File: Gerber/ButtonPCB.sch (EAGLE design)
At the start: 7 parts, among them SW1 SPST_TACT-EVQQ2, SW2 SPST_TACT-EVQQ2, SW3 SPST_TACT-EVQQ2

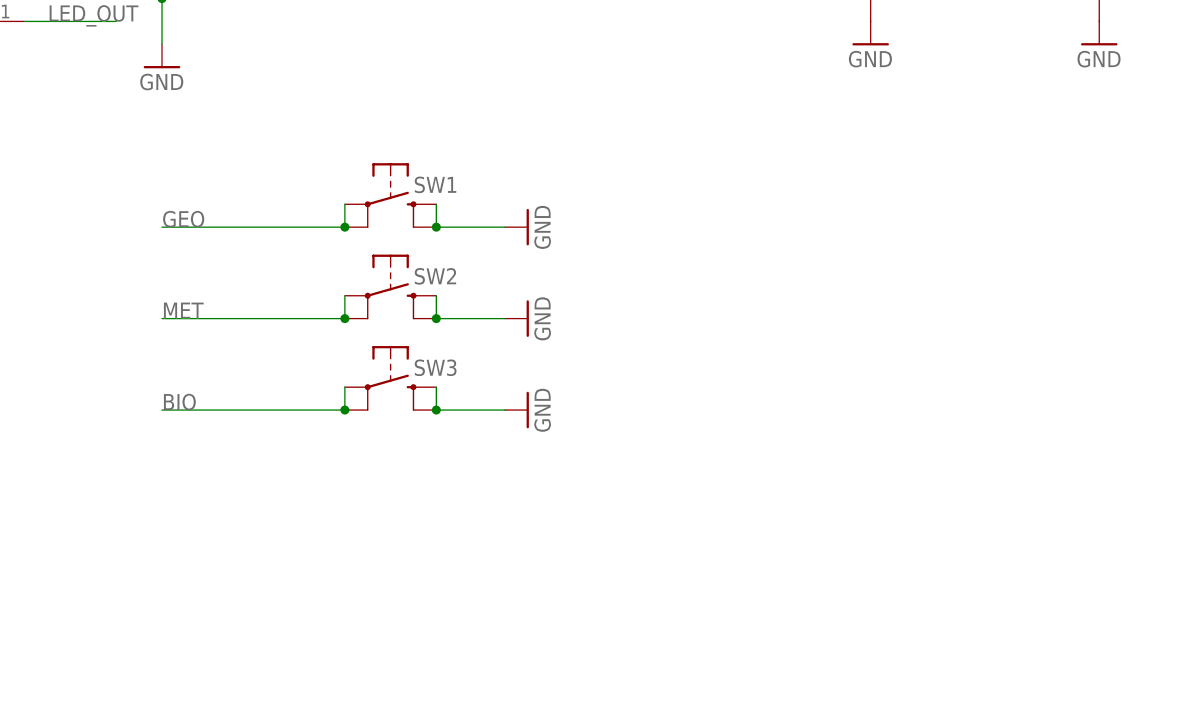
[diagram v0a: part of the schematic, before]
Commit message: Swapped to smd buttons that I like.
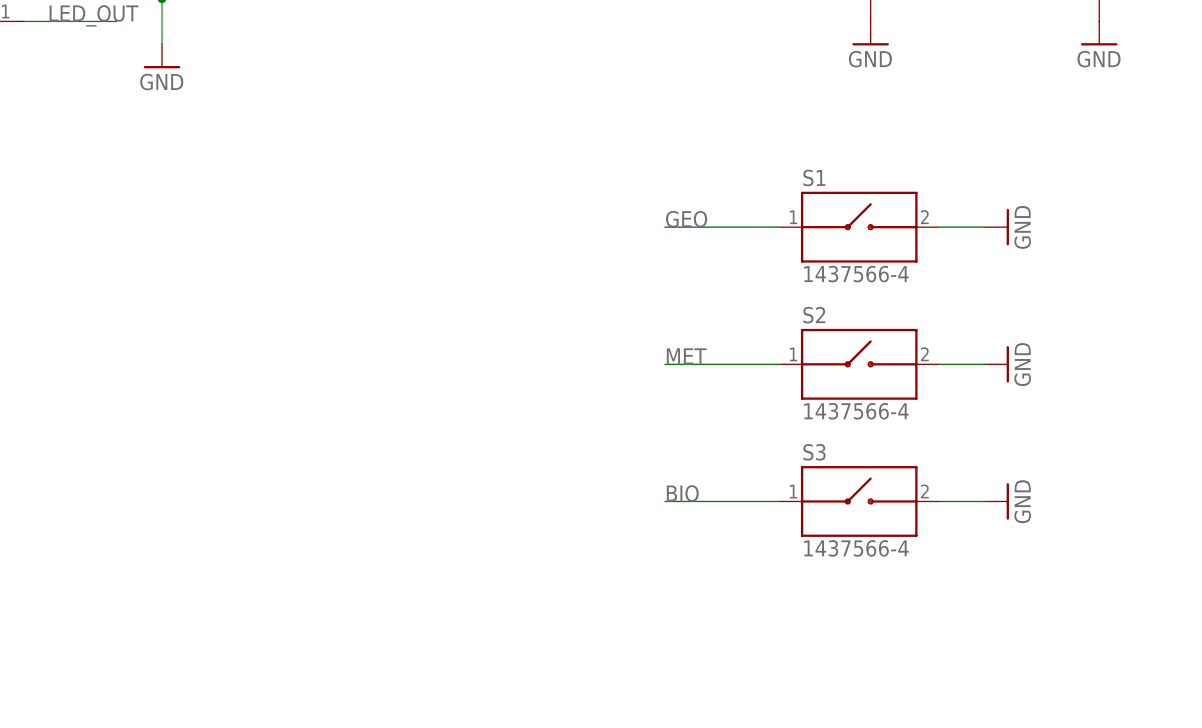
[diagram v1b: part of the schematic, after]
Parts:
- removed SW1, SW2, SW3: SPST_TACT-EVQQ2, microbuilder:SWITCH_TACT_SMT4.6X2.8
- added S1, S2, S3: 1437566-4, FSMSMTR-1437566-4:1437566-4
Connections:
- net BIO: now also S3.1; no longer SW3.P, SW3.P1
- net GEO: now also S1.1; no longer SW1.P, SW1.P1
- net GND: now also S1.2, S2.2, S3.2; no longer SW1.S, SW1.S1, SW2.S, SW2.S1, SW3.S, SW3.S1
- net MET: now also S2.1; no longer SW2.P, SW2.P1
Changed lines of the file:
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@@
 <part name="GND4" library="supply1a" deviceset="GND" device=""/>
 <part name="P+3" library="supply1" deviceset="V+" device=""/>
-<part name="GND22" library="supply1a" deviceset="GND" device=""/>
-<part name="SW1" library="microbuilder" deviceset="SWITCH_TACT_SMT" device="4.6X2.8" value="SPST_TACT-EVQQ2"/>
-<part name="GND1" library="supply1a" deviceset="GND" device=""/>
-<part name="SW2" library="microbuilder" deviceset="SWITCH_TACT_SMT" device="4.6X2.8" value="SPST_TACT-EVQQ2"/>
-<part name="GND2" library="supply1a" deviceset="GND" device=""/>
-<part name="SW3" library="microbuilder" deviceset="SWITCH_TACT_SMT" device="4.6X2.8" value="SPST_TACT-EVQQ2"/>
 <part name="J1" library="SparkFun-Connectors" deviceset="CONN_09" device=""/>
 <part name="P+1" library="supply1" deviceset="V+" device=""/>
 <part name="GND5" library="supply1a" deviceset="GND" device=""/>
+<part name="S1" library="FSMSMTR-1437566-4" deviceset="1437566-4" device=""/>
+<part name="S2" library="FSMSMTR-1437566-4" deviceset="1437566-4" device=""/>
+<part name="S3" library="FSMSMTR-1437566-4" deviceset="1437566-4" device=""/>
+<part name="GND6" library="supply1a" deviceset="GND" device=""/>
+<part name="GND7" library="supply1a" deviceset="GND" device=""/>
+<part name="GND8" library="supply1a" deviceset="GND" device=""/>
 </parts>
 <sheets>
@@
 <attribute name="VALUE" x="182.88" y="160.02" size="1.778" layer="96" rot="R90"/>
 </instance>
-<instance part="GND22" gate="1" x="91.44" y="111.76" smashed="yes" rot="R90">
-<attribute name="VALUE" x="93.98" y="109.22" size="1.778" layer="96" rot="R90"/>
-</instance>
-<instance part="SW1" gate="G$1" x="76.2" y="114.3" smashed="yes">
-<attribute name="NAME" x="78.74" y="115.57" size="1.778" layer="95"/>
-</instance>
-<instance part="GND1" gate="1" x="91.44" y="101.6" smashed="yes" rot="R90">
-<attribute name="VALUE" x="93.98" y="99.06" size="1.778" layer="96" rot="R90"/>
-</instance>
-<instance part="SW2" gate="G$1" x="76.2" y="104.14" smashed="yes">
-<attribute name="NAME" x="78.74" y="105.41" size="1.778" layer="95"/>
-</instance>
-<instance part="GND2" gate="1" x="91.44" y="91.44" smashed="yes" rot="R90">
-<attribute name="VALUE" x="93.98" y="88.9" size="1.778" layer="96" rot="R90"/>
-</instance>
-<instance part="SW3" gate="G$1" x="76.2" y="93.98" smashed="yes">
-<attribute name="NAME" x="78.74" y="95.25" size="1.778" layer="95"/>
-</instance>
 <instance part="J1" gate="J1" x="25.4" y="144.78"/>
 <instance part="P+1" gate="1" x="48.26" y="162.56" smashed="yes">
@@
 <instance part="GND5" gate="1" x="50.8" y="129.54" smashed="yes">
 <attribute name="VALUE" x="48.26" y="127" size="1.778" layer="96"/>
+</instance>
+<instance part="S1" gate="G$1" x="127" y="111.76"/>
+<instance part="S2" gate="G$1" x="127" y="96.52"/>
+<instance part="S3" gate="G$1" x="127" y="81.28"/>
+<instance part="GND6" gate="1" x="144.78" y="111.76" smashed="yes" rot="R90">
+<attribute name="VALUE" x="147.32" y="109.22" size="1.778" layer="96" rot="R90"/>
+</instance>
+<instance part="GND7" gate="1" x="144.78" y="96.52" smashed="yes" rot="R90">
+<attribute name="VALUE" x="147.32" y="93.98" size="1.778" layer="96" rot="R90"/>
+</instance>
+<instance part="GND8" gate="1" x="144.78" y="81.28" smashed="yes" rot="R90">
+<attribute name="VALUE" x="147.32" y="78.74" size="1.778" layer="96" rot="R90"/>
 </instance>
 </instances>
@@
 <pinref part="LED3" gate="G$1" pin="GND"/>
 <pinref part="GND4" gate="1" pin="GND"/>
-</segment>
-<segment>
-<wire x1="88.9" y1="111.76" x2="81.28" y2="111.76" width="0.1524" layer="91"/>
-<wire x1="81.28" y1="114.3" x2="81.28" y2="111.76" width="0.1524" layer="91"/>
-<junction x="81.28" y="111.76"/>
-<pinref part="GND22" gate="1" pin="GND"/>
-<pinref part="SW1" gate="G$1" pin="S"/>
-<pinref part="SW1" gate="G$1" pin="S1"/>
-</segment>
-<segment>
-<wire x1="88.9" y1="101.6" x2="81.28" y2="101.6" width="0.1524" layer="91"/>
-<wire x1="81.28" y1="104.14" x2="81.28" y2="101.6" width="0.1524" layer="91"/>
-<junction x="81.28" y="101.6"/>
-<pinref part="GND1" gate="1" pin="GND"/>
-<pinref part="SW2" gate="G$1" pin="S"/>
-<pinref part="SW2" gate="G$1" pin="S1"/>
-</segment>
-<segment>
-<wire x1="88.9" y1="91.44" x2="81.28" y2="91.44" width="0.1524" layer="91"/>
-<wire x1="81.28" y1="93.98" x2="81.28" y2="91.44" width="0.1524" layer="91"/>
-<junction x="81.28" y="91.44"/>
-<pinref part="GND2" gate="1" pin="GND"/>
-<pinref part="SW3" gate="G$1" pin="S"/>
-<pinref part="SW3" gate="G$1" pin="S1"/>
 </segment>
 <segment>
@@
 <label x="38.1" y="137.16" size="1.778" layer="95"/>
 </segment>
+<segment>
+<pinref part="GND8" gate="1" pin="GND"/>
+<pinref part="S3" gate="G$1" pin="2"/>
+<wire x1="142.24" y1="81.28" x2="137.16" y2="81.28" width="0.1524" layer="91"/>
+</segment>
+<segment>
+<pinref part="S2" gate="G$1" pin="2"/>
+<pinref part="GND7" gate="1" pin="GND"/>
+<wire x1="137.16" y1="96.52" x2="142.24" y2="96.52" width="0.1524" layer="91"/>
+</segment>
+<segment>
+<pinref part="GND6" gate="1" pin="GND"/>
+<pinref part="S1" gate="G$1" pin="2"/>
+<wire x1="142.24" y1="111.76" x2="137.16" y2="111.76" width="0.1524" layer="91"/>
+</segment>
 </net>
 <net name="V+" class="1">
@@
 </segment>
 <segment>
-<pinref part="SW1" gate="G$1" pin="P1"/>
-<pinref part="SW1" gate="G$1" pin="P"/>
-<wire x1="71.12" y1="111.76" x2="71.12" y2="114.3" width="0.1524" layer="91"/>
-<wire x1="71.12" y1="111.76" x2="50.8" y2="111.76" width="0.1524" layer="91"/>
-<junction x="71.12" y="111.76"/>
-<label x="50.8" y="111.76" size="1.778" layer="95"/>
+<wire x1="119.38" y1="111.76" x2="106.68" y2="111.76" width="0.1524" layer="91"/>
+<label x="106.68" y="111.76" size="1.778" layer="95"/>
+<pinref part="S1" gate="G$1" pin="1"/>
 </segment>
 </net>
@@
 </segment>
 <segment>
-<pinref part="SW2" gate="G$1" pin="P1"/>
-<pinref part="SW2" gate="G$1" pin="P"/>
-<wire x1="71.12" y1="101.6" x2="71.12" y2="104.14" width="0.1524" layer="91"/>
-<wire x1="71.12" y1="101.6" x2="50.8" y2="101.6" width="0.1524" layer="91"/>
-<junction x="71.12" y="101.6"/>
-<label x="50.8" y="101.6" size="1.778" layer="95"/>
+<wire x1="119.38" y1="96.52" x2="106.68" y2="96.52" width="0.1524" layer="91"/>
+<label x="106.68" y="96.52" size="1.778" layer="95"/>
+<pinref part="S2" gate="G$1" pin="1"/>
 </segment>
 </net>
@@
 </segment>
 <segment>
-<pinref part="SW3" gate="G$1" pin="P1"/>
-<pinref part="SW3" gate="G$1" pin="P"/>
-<wire x1="71.12" y1="91.44" x2="71.12" y2="93.98" width="0.1524" layer="91"/>
-<wire x1="71.12" y1="91.44" x2="50.8" y2="91.44" width="0.1524" layer="91"/>
-<junction x="71.12" y="91.44"/>
-<label x="50.8" y="91.44" size="1.778" layer="95"/>
-</segment>
-</net>
+<wire x1="119.38" y1="81.28" x2="106.68" y2="81.28" width="0.1524" layer="91"/>
+<label x="106.68" y="81.28" size="1.778" layer="95"/>
+<pinref part="S3" gate="G$1" pin="1"/>
+</segment>
+</net>

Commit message: minor updates, notes
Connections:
- net BIO renamed BIO_BUTTON
- net GEO renamed GEO_BUTTON
- net MET renamed MET_BUTTON
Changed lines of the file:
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@@
 </segment>
 </net>
-<net name="GEO" class="0">
+<net name="GEO_BUTTON" class="0">
 <segment>
 <pinref part="J1" gate="J1" pin="6"/>
@@
 </segment>
 </net>
-<net name="MET" class="0">
+<net name="MET_BUTTON" class="0">
 <segment>
 <pinref part="J1" gate="J1" pin="5"/>
@@
 </segment>
 </net>
-<net name="BIO" class="0">
+<net name="BIO_BUTTON" class="0">
 <segment>
 <pinref part="J1" gate="J1" pin="4"/>
